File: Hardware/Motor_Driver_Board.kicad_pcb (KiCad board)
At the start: 2 copper layers, 63.8 x 52.5 mm, 36 parts, among them J1 POWER, J2 MOTOR, J3 LCD, SW1 ENCODER, U1 XL1509-5.0

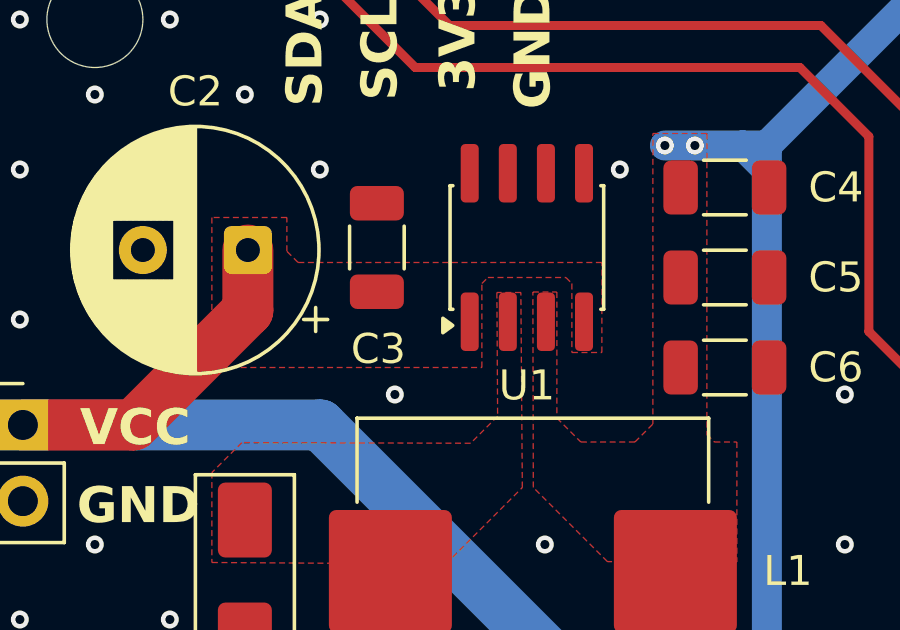
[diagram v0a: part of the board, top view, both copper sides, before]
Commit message: Structure and software
Updated the project structure.
Added an initial software for the board.
Fixed minor errors on the PCB.
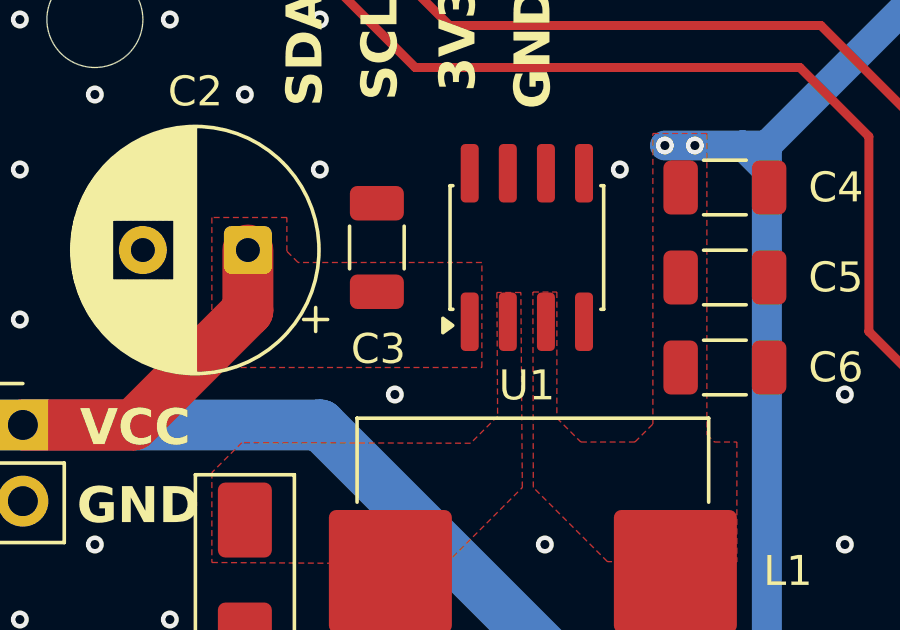
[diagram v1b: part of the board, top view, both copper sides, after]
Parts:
- R10, R11: value 10K -> 2.2K
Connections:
- U1 pad 4: VCC -> GND
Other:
- board text added: "V1.0 REV B PD 05/26 RYAN WANG DAVID MT"
- board text removed: "V1.0 REV A PD 05/26 RYAN WANG DAVID MT"
